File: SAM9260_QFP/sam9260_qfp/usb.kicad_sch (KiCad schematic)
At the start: 51 parts, among them J301 USB_A, J302 USB_A, U301 USBLC6-2SC6, U302 USB2514B_Bi, U303 MIC2099-1YMT-TR, U304 MIC2099-1YMT-TR, U305 USBLC6-2SC6, U306 USBLC6-2SC6, Y301 24MHz

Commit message: Completed component placing
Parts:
- FB301, FB302, FB303: footprint Inductor_SMD:L_0805_2012Metric -> Inductor_SMD:L_0603_1608Metric
- U303, U304: footprint My_First_PCB:TMLF-6_MT_MCH -> MIC2099:TMLF-6_MT_MCH

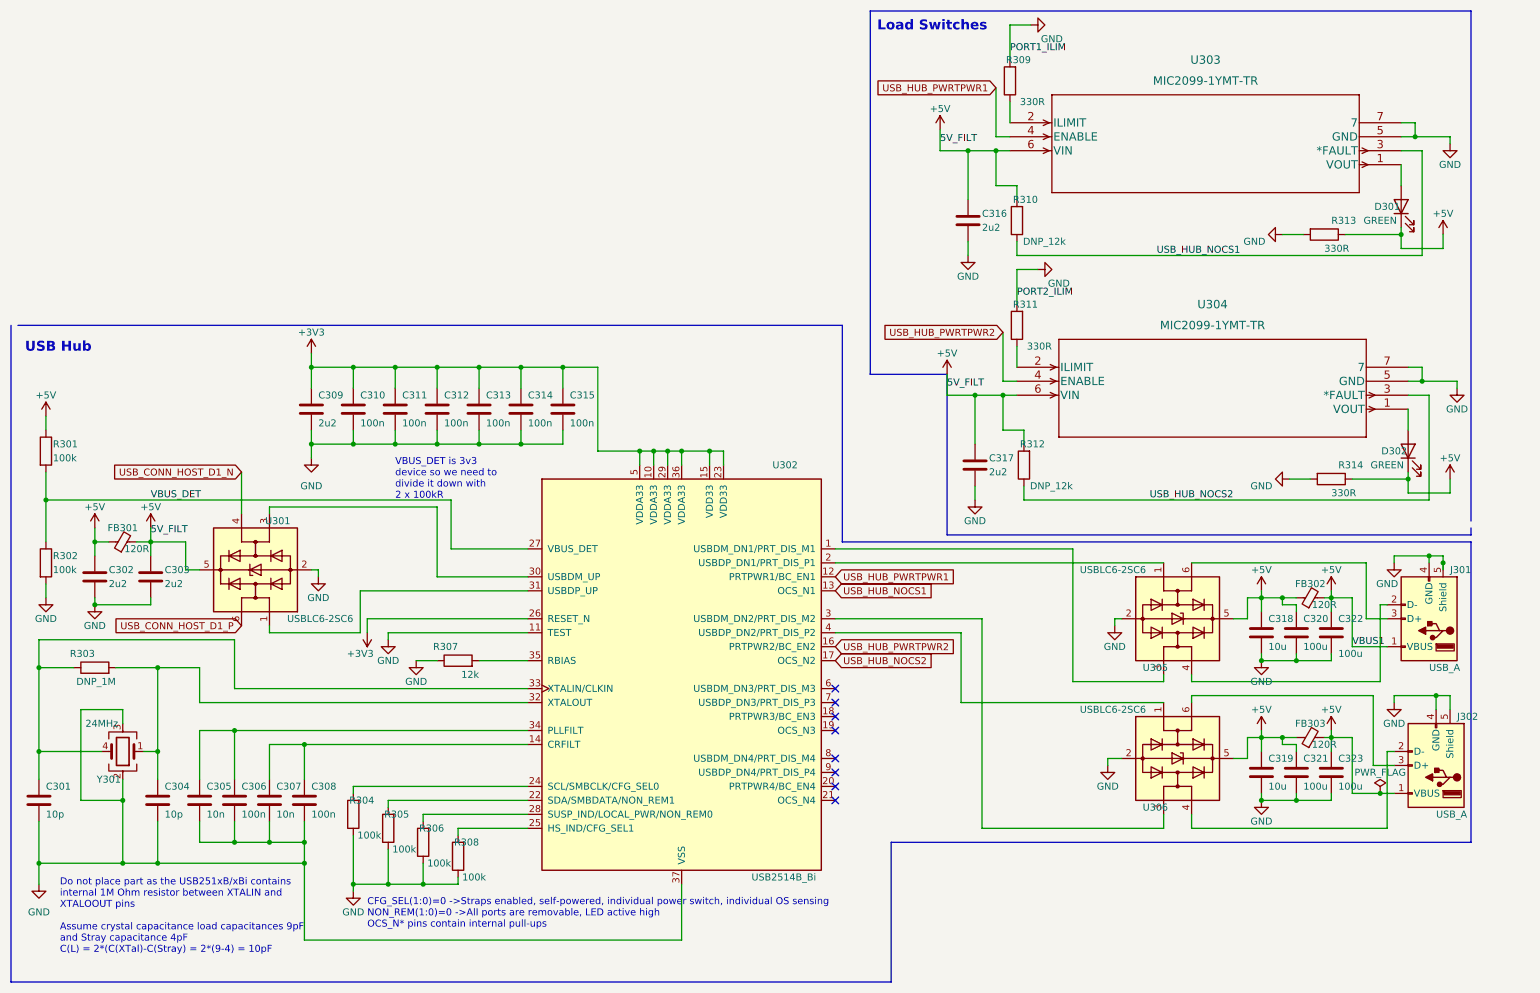
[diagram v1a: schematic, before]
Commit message: updated layout
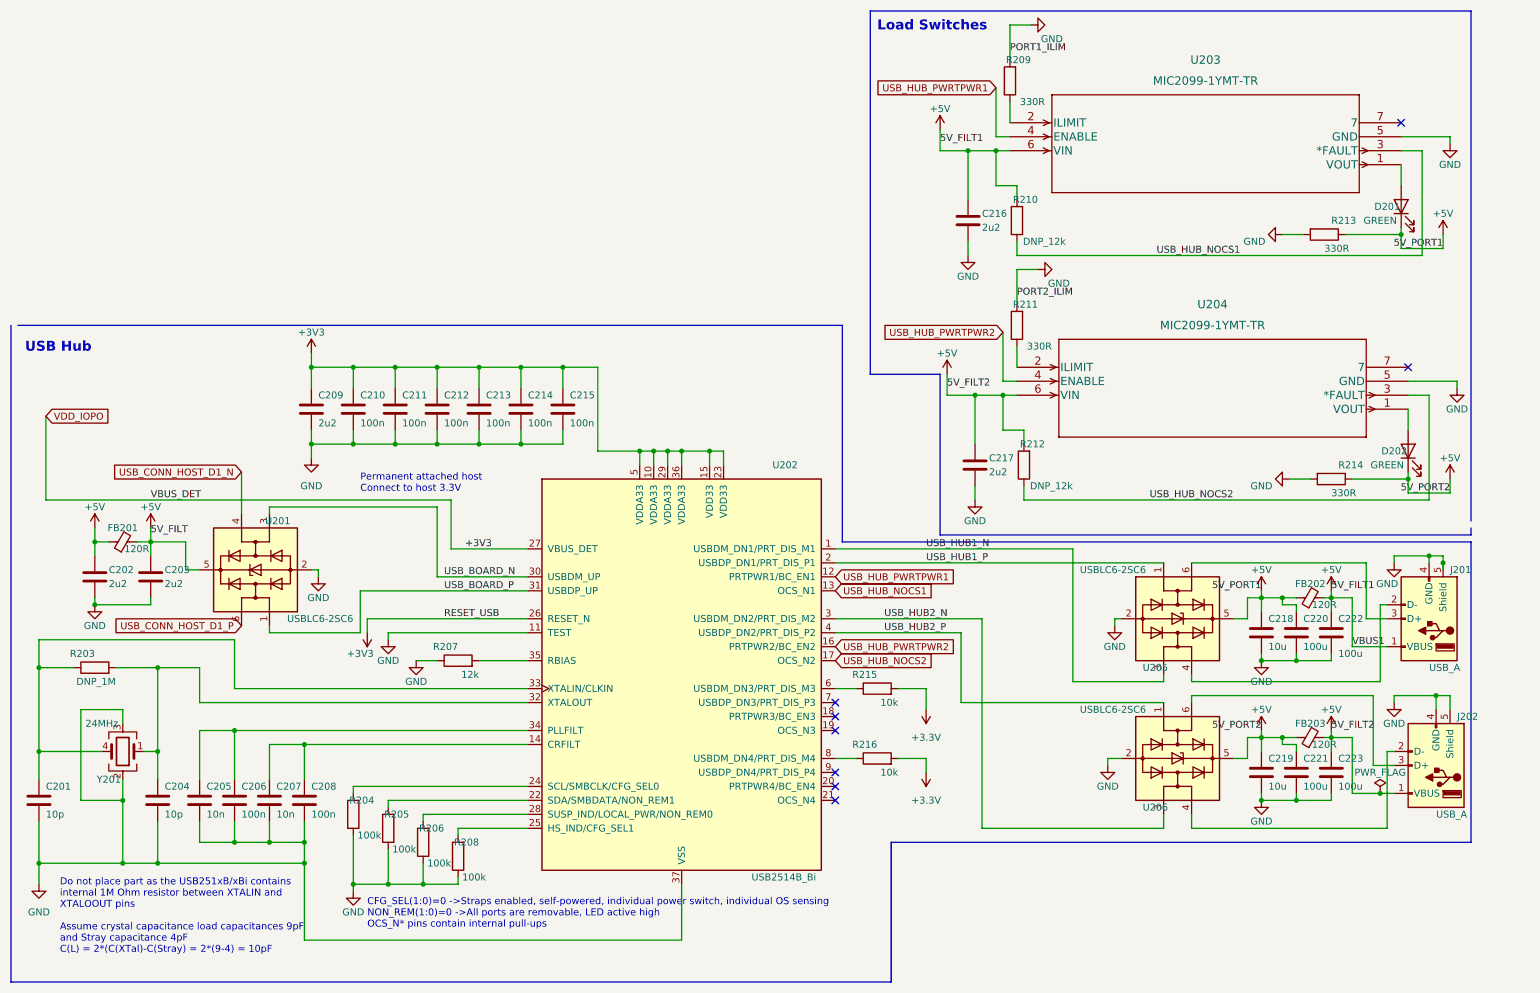
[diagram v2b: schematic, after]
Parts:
- removed R301, R302: 100k, Resistor_SMD:R_0603_1608Metric, symbol Device:R
- added R215, R216: 10k, Resistor_SMD:R_0603_1608Metric, symbol Device:R
- renumbered C301 to C201, C302 to C202, C303 to C203, C304 to C204, C305 to C205, C306 to C206, C307 to C207, C308 to C208, C309 to C209, C310 to C210, C311 to C211, C312 to C212, C313 to C213, C314 to C214, C315 to C215, C316 to C216, C317 to C217, C318 to C218, C319 to C219, C320 to C220, C321 to C221, C322 to C222, C323 to C223, D301 to D201, D302 to D202, FB301 to FB201, FB302 to FB202, FB303 to FB203, J301 to J201, J302 to J202, R303 to R203, R304 to R204, R305 to R205, R306 to R206, R307 to R207, R308 to R208, R309 to R209, R310 to R210, R311 to R211, R312 to R212, R313 to R213, R314 to R214, U301 to U201, U302 to U202, U303 to U203, U304 to U204, U305 to U205, U306 to U206, Y301 to Y201
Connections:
- net VBUS_DET is gone; now on net +3V3: U202.27 (VBUS_DET)
- net GND: no longer U203.7, U204.7
- net USB_BOARD_P: now reaches U201.1 (I/O1), U202.31 (USBDP_UP)
- net USB_BOARD_N: now reaches U201.3 (I/O2), U202.30 (USBDM_UP)
- net USB_HUB1_P: now reaches U202.2 (USBDP_DN1/PRT_DIS_P1), U205.1 (I/O1)
- net USB_HUB1_N: now reaches U202.1 (USBDM_DN1/PRT_DIS_M1), U205.3 (I/O2)
- net USB_HUB2_N: now reaches U202.3 (USBDM_DN2/PRT_DIS_M2), U206.3 (I/O2)
- net USB_HUB2_P: now reaches U202.4 (USBDP_DN2/PRT_DIS_P2), U206.1 (I/O1)
- net at U202.6 (USBDM_DN3/PRT_DIS_M3): now also R215.1
- net at U202.8 (USBDM_DN4/PRT_DIS_M4): now also R216.1
- new net +3.3V: R215.2, R216.2
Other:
- note added: "Permanent attached host Connect to host 3.3V"
- note removed: "VBUS_DET is 3v3 device so we need to divide it down with 2 x 100kR"

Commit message: Completed routing, need to add logo
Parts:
- removed R210, R212: DNP_12k, Resistor_SMD:R_0603_1608Metric, symbol Device:R
- removed R213, R214: 330R, Resistor_SMD:R_0402_1005Metric, symbol Device:R
- added C224, C225: 2u2, Capacitor_SMD:C_0603_1608Metric, symbol Device:C
- added R201, R202: 330R, Resistor_SMD:R_0402_1005Metric, symbol Device:R
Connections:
- net +3V3: now also C202.1, C216.1, C217.1, C222.1, C223.1, FB201.1, FB202.2, FB203.2, J201.1 (VBUS), J202.1 (VBUS), U203.6 (VIN), U204.6 (VIN)
- net GND: now also C224.2, C225.2, R201.1, R202.1
- net 3V3_PORT1: now reaches D201.2 (A), U203.1 (VOUT)
- net 3V3_PORT1: now also C218.1, C220.1, FB202.1, U205.5 (VBUS), C224.1
- net 3V3_PORT2: now reaches D202.2 (A), U204.1 (VOUT)
- net 3V3_PORT2: now also C219.1, C221.1, FB203.1, U206.5 (VBUS), C225.1
- removed net +5V: C202.1, C203.1, C216.1, C217.1, C218.1, C219.1, C220.1, C221.1, C222.1, C223.1, D201.1 (K), D202.1 (K), FB201.1, FB201.2, FB202.1, FB202.2, FB203.1, FB203.2, J201.1 (VBUS), J202.1 (VBUS), U201.5 (VBUS), U203.6 (VIN), U204.6 (VIN), U205.5 (VBUS), U206.5 (VBUS)
- new net: C203.1, FB201.2, U201.5 (VBUS)
- new net: D201.1 (K), R201.2
- new net: D202.1 (K), R202.2
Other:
- note added: "NFAULT->Logic low = over-current/thermal protection engaged R(ILM)=330R -> I(LIM)~=450mA to 750mA"
- moved on the sheet: C217, D201, D202, R211, U204
